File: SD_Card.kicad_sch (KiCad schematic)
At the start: 1 part, among them J13 Micro_SD_Card

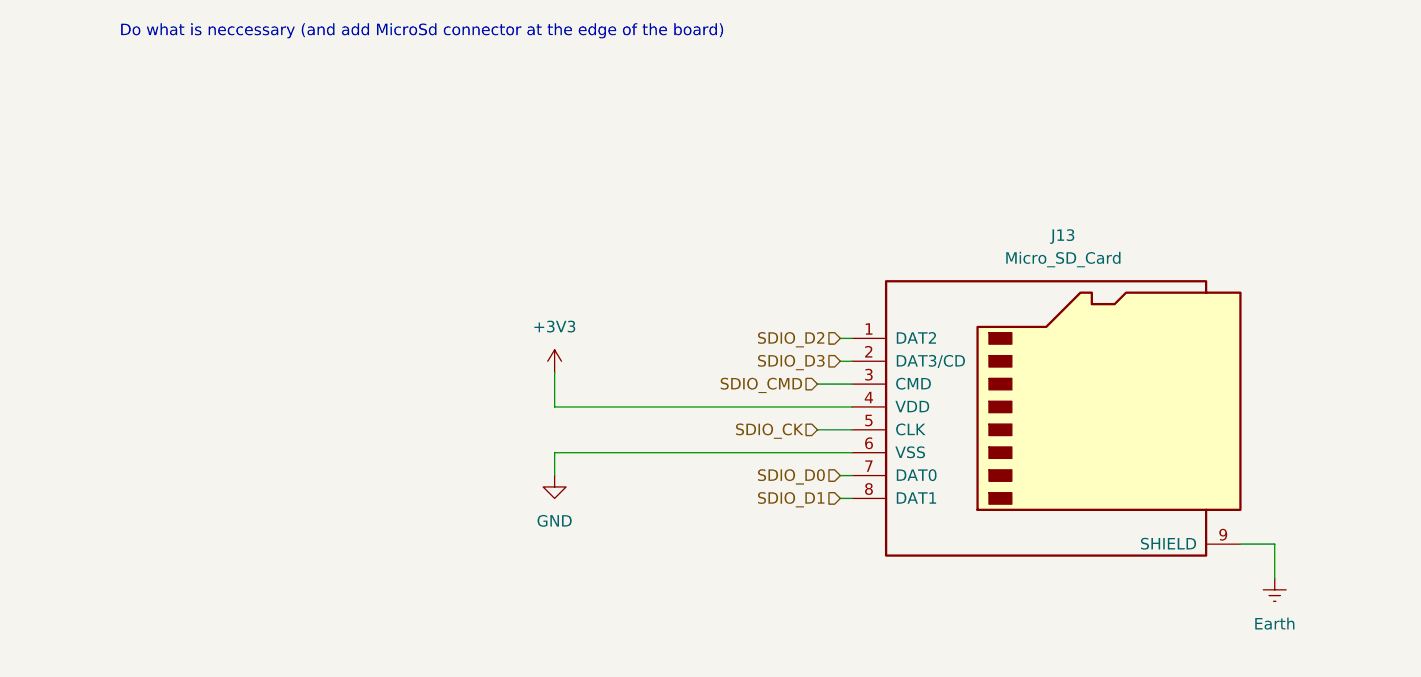
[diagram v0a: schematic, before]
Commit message: Key CHanges for connector choices , termination and semi-final decisions on them
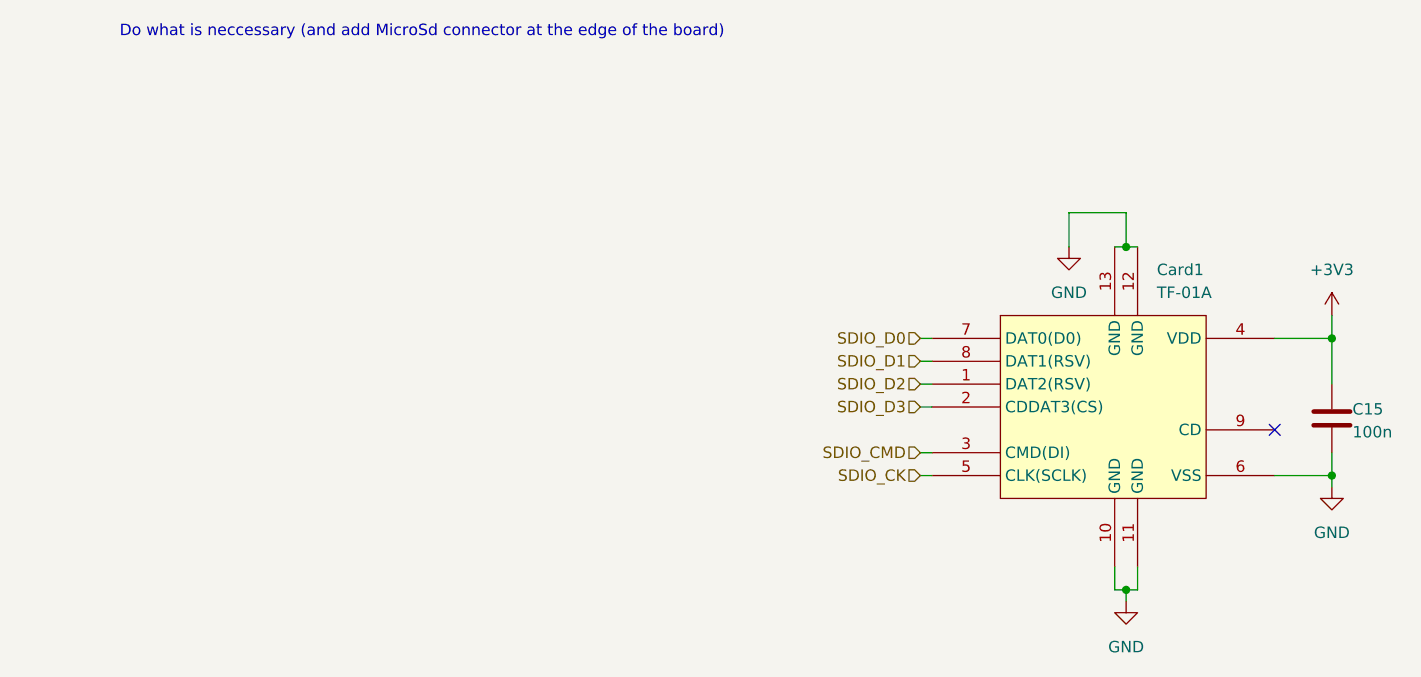
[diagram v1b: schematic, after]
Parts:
- removed J13: Micro_SD_Card, Connector_Card:microSD_HC_Molex_47219-2001, symbol Connector:Micro_SD_Card
- added C15: 100n, Capacitor_SMD:C_0805_2012Metric, symbol Device:C
- added Card1: TF-01A, EasyEDA:TF-SMD_TF-01A, symbol EasyEDA:TF-01A
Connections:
- net +3V3: now also C15.1, Card1.4 (VDD)
- net GND: now also C15.2, Card1.10 (GND), Card1.11 (GND), Card1.12 (GND), Card1.13 (GND), Card1.6 (VSS)
- net SDIO_CK: now also Card1.5 (CLK(SCLK))
- net SDIO_CMD: now also Card1.3 (CMD(DI))
- net SDIO_D0: now also Card1.7 (DAT0(D0))
- net SDIO_D1: now also Card1.8 (DAT1(RSV))
- net SDIO_D2: now also Card1.1 (DAT2(RSV))
- net SDIO_D3: now also Card1.2 (CDDAT3(CS))
- no-connect marks 0 -> 1
